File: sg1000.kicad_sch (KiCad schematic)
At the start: 76 parts, among them CN1 Conn_01x07_Female, J1 USB-B1HSB6, J2 RCJ-014, J3 RCJ-013, Q1 2n4401, Q1c1 2n3906, SW1 Pause Key, SW2 Power Toggle, SW3 Reset Key, U1 SG-1000-Cart, U100 74HCT574, U101 74HCT574, U102 74HCT574, U103 AS6C62256-DIP, U11 AS6C62256-DIP, U12 TMS9918A, U13 74LS139, U16 74LS32, U17 74LS14, U18 74LS257, U2 SG-1000-Expansion, U21 74LS257, U3 SN76489AN, U4 74LS32, U5 27C256, U6 74LS573, U7 74LS00, U9 Z80CPU, U99 74HCT04, X2 10.73863MHz

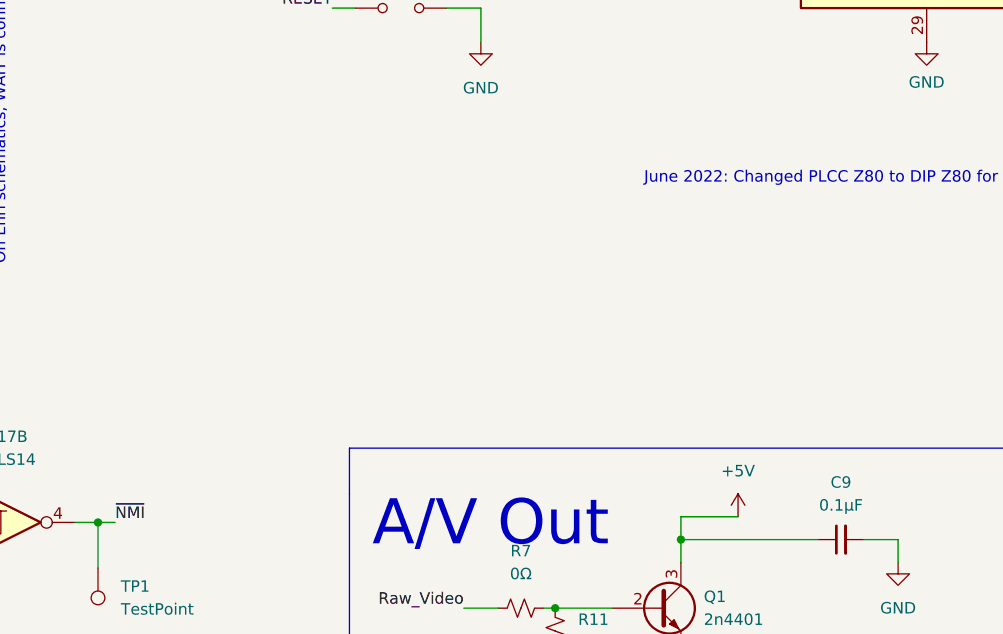
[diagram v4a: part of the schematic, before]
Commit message: Ground unused Schmitt trigger inputs
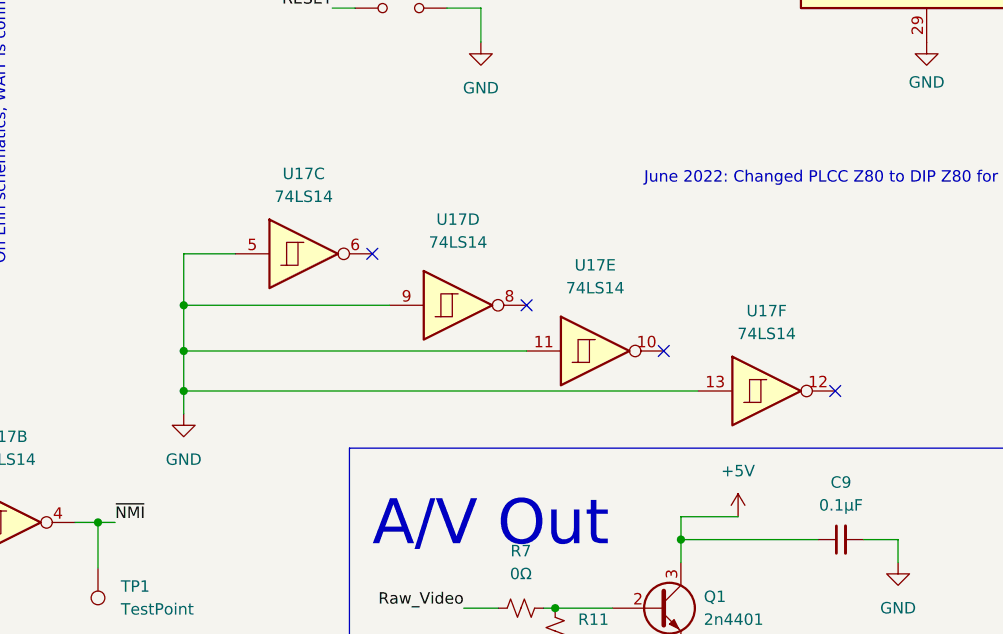
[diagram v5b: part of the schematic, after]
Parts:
- added unit 4 of U17
- added unit 6 of U17
- added unit 3 of U17
- added unit 5 of U17
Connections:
- net GND: now also U17.11, U17.13, U17.5, U17.9
- no-connect marks 25 -> 29
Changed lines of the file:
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@@
   (junction (at 219.71 165.735) (diameter 0) (color 0 0 0 0)
   )
+  (junction (at 229.235 146.685) (diameter 0) (color 0 0 0 0)
+  )
+  (junction (at 229.235 141.605) (diameter 0) (color 0 0 0 0)
+  )
   (junction (at 191.135 101.6) (diameter 0) (color 0 0 0 0)
   )
@@
   (junction (at 237.49 69.215) (diameter 0) (color 0 0 0 0)
   )
+  (junction (at 229.235 151.13) (diameter 0) (color 0 0 0 0)
+  )
   (junction (at 45.085 81.28) (diameter 0) (color 0 0 0 0)
   )
@@
   (no_connect (at 417.83 43.18))
   (no_connect (at 65.405 455.93))
+  (no_connect (at 282.575 146.685))
+  (no_connect (at 301.625 151.13))
+  (no_connect (at 267.335 141.605))
+  (no_connect (at 250.19 135.89))
   (no_connect (at 65.405 440.69))
   (no_connect (at 294.005 104.775))
@@
     (stroke (width 0) (type default) (color 0 0 0 0))
   )
+  (wire (pts (xy 229.235 135.89) (xy 229.235 141.605))
+    (stroke (width 0) (type default) (color 0 0 0 0))
+  )
   (wire (pts (xy 71.755 673.735) (xy 78.105 673.735))
     (stroke (width 0) (type default) (color 0 0 0 0))
@@
     (stroke (width 0) (type default) (color 0 0 0 0))
   )
+  (wire (pts (xy 229.235 151.13) (xy 286.385 151.13))
+    (stroke (width 0) (type default) (color 0 0 0 0))
+  )
   (wire (pts (xy 133.35 322.58) (xy 138.43 322.58))
     (stroke (width 0) (type default) (color 0 0 0 0))
@@
     (stroke (width 0) (type default) (color 0 0 0 0))
   )
+  (wire (pts (xy 234.95 135.89) (xy 229.235 135.89))
+    (stroke (width 0) (type default) (color 0 0 0 0))
+  )
   (wire (pts (xy 66.04 534.67) (xy 73.66 534.67))
     (stroke (width 0) (type default) (color 0 0 0 0))
   )
+  (wire (pts (xy 229.235 141.605) (xy 252.095 141.605))
+    (stroke (width 0) (type default) (color 0 0 0 0))
+  )
   (wire (pts (xy 60.96 40.005) (xy 55.245 40.005))
     (stroke (width 0) (type default) (color 0 0 0 0))
@@
     (stroke (width 0) (type default) (color 0 0 0 0))
   )
+  (wire (pts (xy 229.235 151.13) (xy 229.235 153.67))
+    (stroke (width 0) (type default) (color 0 0 0 0))
+  )
   (wire (pts (xy 149.225 746.125) (xy 149.225 748.665))
     (stroke (width 0) (type default) (color 0 0 0 0))
@@
     (stroke (width 0) (type default) (color 0 0 0 0))
   )
+  (wire (pts (xy 229.235 146.685) (xy 229.235 151.13))
+    (stroke (width 0) (type default) (color 0 0 0 0))
+  )
   (wire (pts (xy 269.24 175.26) (xy 270.51 175.26))
     (stroke (width 0) (type default) (color 0 0 0 0))
@@
     (stroke (width 0) (type default) (color 0 0 0 0))
   )
+  (wire (pts (xy 229.235 141.605) (xy 229.235 146.685))
+    (stroke (width 0) (type default) (color 0 0 0 0))
+  )
   (wire (pts (xy 153.67 443.23) (xy 137.795 443.23))
     (stroke (width 0) (type default) (color 0 0 0 0))
@@
     (stroke (width 0) (type default) (color 0 0 0 0))
   )
+  (wire (pts (xy 229.235 146.685) (xy 267.335 146.685))
+    (stroke (width 0) (type default) (color 0 0 0 0))
+  )
   (wire (pts (xy 43.815 668.655) (xy 51.435 668.655))
     (stroke (width 0) (type default) (color 0 0 0 0))
@@
     (pin "2")
   )
+  (symbol (lib_id "power:GND") (at 229.235 153.67 0) (unit 1)
+    (in_bom yes) (on_board yes) (fields_autoplaced)
+    (property "Reference" "#PWR?" (id 0) (at 229.235 160.02 0)
+      (effects (font (size 1.27 1.27)) hide)
+    )
+    (property "Value" "GND" (id 1) (at 229.235 158.75 0))
+    (property "Footprint" "" (id 2) (at 229.235 153.67 0)
+      (effects (font (size 1.27 1.27)) hide)
+    )
+    (property "Datasheet" "" (id 3) (at 229.235 153.67 0)
+      (effects (font (size 1.27 1.27)) hide)
+    )
+    (pin "1")
+  )
   (symbol (lib_id "power:+5V") (at 106.045 186.055 0) (unit 1)
     (in_bom yes) (on_board yes) (fields_autoplaced)
@@
     (pin "2")
   )
+  (symbol (lib_id "74xx:74LS14") (at 259.715 141.605 0) (unit 4)
+    (in_bom yes) (on_board yes) (fields_autoplaced)
+    (property "Reference" "U17" (id 0) (at 259.715 132.08 0))
+    (property "Value" "74LS14" (id 1) (at 259.715 134.62 0))
+    (property "Footprint" "" (id 2) (at 259.715 141.605 0)
+      (effects (font (size 1.27 1.27)) hide)
+    )
+    (property "Datasheet" "http://www.ti.com/lit/gpn/sn74LS14" (id 3) (at 259.715 141.605 0)
+      (effects (font (size 1.27 1.27)) hide)
+    )
+    (pin "8")
+    (pin "9")
+  )
   (symbol (lib_id "Device:R_Small_US") (at 450.85 58.42 90) (unit 1)
     (in_bom yes) (on_board yes) (fields_autoplaced)
@@
     (pin "2")
   )
+  (symbol (lib_id "74xx:74LS14") (at 294.005 151.13 0) (unit 6)
+    (in_bom yes) (on_board yes) (fields_autoplaced)
+    (property "Reference" "U17" (id 0) (at 294.005 142.24 0))
+    (property "Value" "74LS14" (id 1) (at 294.005 144.78 0))
+    (property "Footprint" "" (id 2) (at 294.005 151.13 0)
+      (effects (font (size 1.27 1.27)) hide)
+    )
+    (property "Datasheet" "http://www.ti.com/lit/gpn/sn74LS14" (id 3) (at 294.005 151.13 0)
+      (effects (font (size 1.27 1.27)) hide)
+    )
+    (pin "12")
+    (pin "13")
+  )
   (symbol (lib_id "power:+5V") (at 308.61 31.75 0) (unit 1)
     (in_bom yes) (on_board yes) (fields_autoplaced)
@@
     (pin "1")
   )
+  (symbol (lib_id "74xx:74LS14") (at 242.57 135.89 0) (unit 3)
+    (in_bom yes) (on_board yes) (fields_autoplaced)
+    (property "Reference" "U17" (id 0) (at 242.57 127 0))
+    (property "Value" "74LS14" (id 1) (at 242.57 129.54 0))
+    (property "Footprint" "" (id 2) (at 242.57 135.89 0)
+      (effects (font (size 1.27 1.27)) hide)
+    )
+    (property "Datasheet" "http://www.ti.com/lit/gpn/sn74LS14" (id 3) (at 242.57 135.89 0)
+      (effects (font (size 1.27 1.27)) hide)
+    )
+    (pin "5")
+    (pin "6")
+  )
   (symbol (lib_id "Device:R_Small_US") (at 284.48 185.42 0) (unit 1)
     (in_bom yes) (on_board yes) (fields_autoplaced)
@@
     (pin "2")
   )
+  (symbol (lib_id "74xx:74LS14") (at 274.955 146.685 0) (unit 5)
+    (in_bom yes) (on_board yes) (fields_autoplaced)
+    (property "Reference" "U17" (id 0) (at 274.955 137.16 0))
+    (property "Value" "74LS14" (id 1) (at 274.955 139.7 0))
+    (property "Footprint" "" (id 2) (at 274.955 146.685 0)
+      (effects (font (size 1.27 1.27)) hide)
+    )
+    (property "Datasheet" "http://www.ti.com/lit/gpn/sn74LS14" (id 3) (at 274.955 146.685 0)
+      (effects (font (size 1.27 1.27)) hide)
+    )
+    (pin "10")
+    (pin "11")
+  )
   (symbol (lib_id "74xx:74LS32") (at 100.965 601.345 0) (unit 3)
     (in_bom yes) (on_board yes) (fields_autoplaced)
@@
       (reference "#PWR0169") (unit 1) (value "GND") (footprint "")
     )
+    (path "/0e0f72eb-ced8-432d-b843-913cc8b0c274"
+      (reference "#PWR?") (unit 1) (value "GND") (footprint "")
+    )
     (path "/00000000-0000-0000-0000-00005e7d9a30"
       (reference "C1") (unit 1) (value "0.1µF") (footprint "Capacitor_SMD:C_0805_2012Metric_Pad1.15x1.40mm_HandSolder")
@@
       (reference "U17") (unit 2) (value "74LS14") (footprint "Package_DIP:DIP-14_W7.62mm_Socket_LongPads")
     )
+    (path "/9890ab0d-60be-401f-9610-601b07554a6a"
+      (reference "U17") (unit 3) (value "74LS14") (footprint "")
+    )
+    (path "/6402a45e-5c18-4acb-95d5-4d4add53b62f"
+      (reference "U17") (unit 4) (value "74LS14") (footprint "")
+    )
+    (path "/cabad2b3-d478-4de3-8c0a-6aca87ea2c66"
+      (reference "U17") (unit 5) (value "74LS14") (footprint "")
+    )
+    (path "/8e7b1928-223e-47d4-86c0-186f141f0453"
+      (reference "U17") (unit 6) (value "74LS14") (footprint "")
+    )
     (path "/7694c0b2-929f-4a6b-9d1a-50ef57c75725"

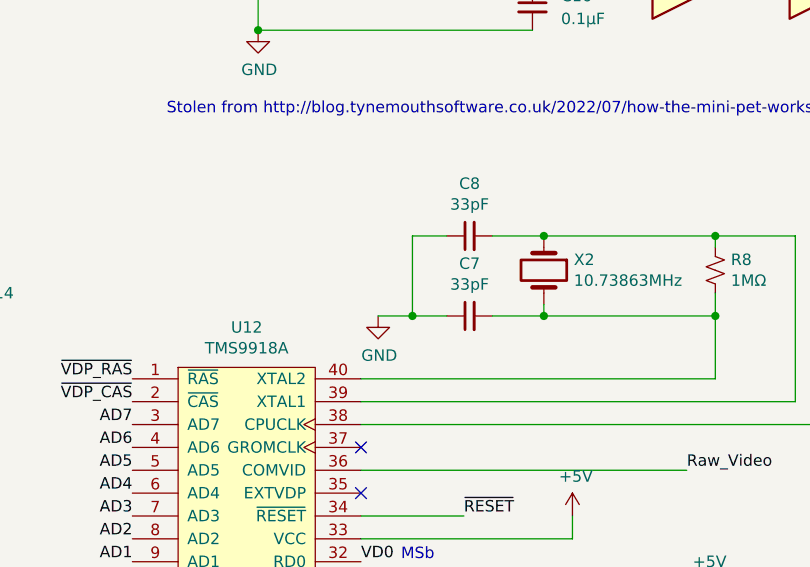
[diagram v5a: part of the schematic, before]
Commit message: Trim cap for clock crystal
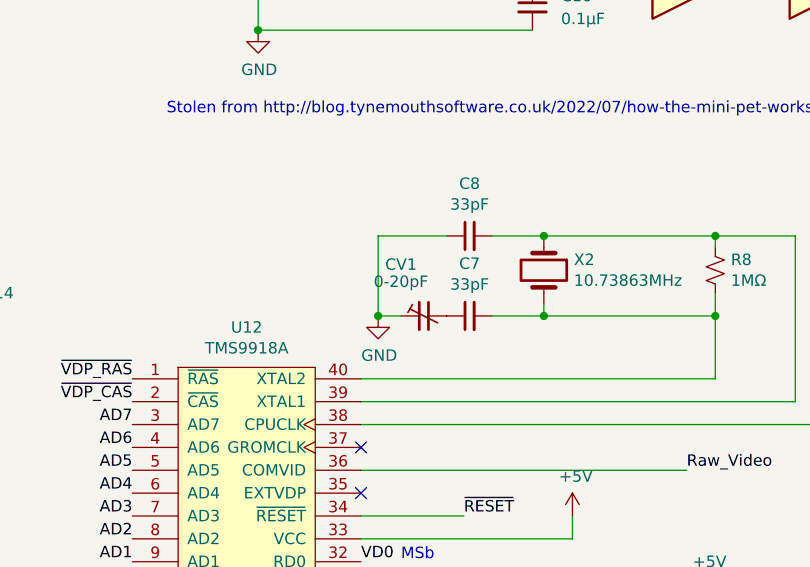
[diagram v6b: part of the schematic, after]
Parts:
- added CV1: 0-20pF, LeadedSolder:Tayda_Variable_Trimmer_Cap, symbol Device:C_Trim_Small
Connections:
- net GND: now also CV1.1; no longer C7.1
- new net: C7.1, CV1.2
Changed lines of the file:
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@@
   (junction (at 114.3 466.725) (diameter 0) (color 0 0 0 0)
   )
+  (junction (at 160.02 202.565) (diameter 0) (color 0 0 0 0)
+  )
   (junction (at 270.51 175.26) (diameter 0) (color 0 0 0 0)
   )
@@
   (junction (at 434.34 58.42) (diameter 0) (color 0 0 0 0)
   )
-  (junction (at 163.83 202.565) (diameter 0) (color 0 0 0 0)
-  )
   (junction (at 439.42 54.61) (diameter 0) (color 0 0 0 0)
   )
@@
     (stroke (width 0) (type default) (color 0 0 0 0))
   )
-  (wire (pts (xy 163.83 202.565) (xy 163.83 193.675))
-    (stroke (width 0) (type default) (color 0 0 0 0))
-  )
   (wire (pts (xy 25.4 182.245) (xy 29.21 182.245))
     (stroke (width 0) (type default) (color 0 0 0 0))
@@
     (stroke (width 0) (type default) (color 0 0 0 0))
   )
+  (wire (pts (xy 160.02 193.675) (xy 160.02 202.565))
+    (stroke (width 0) (type default) (color 0 0 0 0))
+  )
   (wire (pts (xy 464.82 58.42) (xy 458.47 58.42))
     (stroke (width 0) (type default) (color 0 0 0 0))
@@
     (stroke (width 0) (type default) (color 0 0 0 0))
   )
+  (wire (pts (xy 160.02 193.675) (xy 167.64 193.675))
+    (stroke (width 0) (type default) (color 0 0 0 0))
+  )
   (wire (pts (xy 35.56 547.37) (xy 43.18 547.37))
     (stroke (width 0) (type default) (color 0 0 0 0))
@@
     (stroke (width 0) (type default) (color 0 0 0 0))
   )
+  (wire (pts (xy 160.02 202.565) (xy 162.56 202.565))
+    (stroke (width 0) (type default) (color 0 0 0 0))
+  )
   (wire (pts (xy 270.51 175.26) (xy 276.86 175.26))
     (stroke (width 0) (type default) (color 0 0 0 0))
@@
     (stroke (width 0) (type default) (color 0 0 0 0))
   )
-  (wire (pts (xy 163.83 193.675) (xy 167.64 193.675))
-    (stroke (width 0) (type default) (color 0 0 0 0))
-  )
   (wire (pts (xy 155.575 396.24) (xy 166.37 396.24))
     (stroke (width 0) (type default) (color 0 0 0 0))
@@
     (stroke (width 0) (type default) (color 0 0 0 0))
   )
-  (wire (pts (xy 160.02 202.565) (xy 163.83 202.565))
-    (stroke (width 0) (type default) (color 0 0 0 0))
-  )
   (wire (pts (xy 71.755 658.495) (xy 78.105 658.495))
     (stroke (width 0) (type default) (color 0 0 0 0))
@@
     (stroke (width 0) (type default) (color 0 0 0 0))
   )
-  (wire (pts (xy 163.83 202.565) (xy 167.64 202.565))
-    (stroke (width 0) (type default) (color 0 0 0 0))
-  )
   (wire (pts (xy 170.18 78.74) (xy 167.005 78.74))
     (stroke (width 0) (type default) (color 0 0 0 0))
@@
   (symbol (lib_id "power:GND") (at 229.235 153.67 0) (unit 1)
     (in_bom yes) (on_board yes) (fields_autoplaced)
-    (property "Reference" "#PWR?" (id 0) (at 229.235 160.02 0)
+    (property "Reference" "#PWR0151" (id 0) (at 229.235 160.02 0)
       (effects (font (size 1.27 1.27)) hide)
     )
@@
     (pin "1")
   )
+  (symbol (lib_id "Device:C_Trim_Small") (at 165.1 202.565 90) (unit 1)
+    (in_bom yes) (on_board yes)
+    (property "Reference" "CV1" (id 0) (at 162.56 196.85 90))
+    (property "Value" "0-20pF" (id 1) (at 162.56 198.755 90))
+    (property "Footprint" "LeadedSolder:Tayda_Variable_Trimmer_Cap" (id 2) (at 165.1 202.565 0)
+      (effects (font (size 1.27 1.27)) hide)
+    )
+    (property "Datasheet" "~" (id 3) (at 165.1 202.565 0)
+      (effects (font (size 1.27 1.27)) hide)
+    )
+    (pin "1")
+    (pin "2")
+  )
   (symbol (lib_id "power:GND") (at 44.45 715.01 0) (unit 1)
     (in_bom yes) (on_board yes) (fields_autoplaced)
@@
       (reference "#PWR0150") (unit 1) (value "+5V") (footprint "")
     )
+    (path "/0e0f72eb-ced8-432d-b843-913cc8b0c274"
+      (reference "#PWR0151") (unit 1) (value "GND") (footprint "")
+    )
     (path "/7fa93b8d-6199-40ac-a4b9-d0ffd76e76bb"
       (reference "#PWR0152") (unit 1) (value "+5V") (footprint "")
@@
       (reference "#PWR0169") (unit 1) (value "GND") (footprint "")
     )
-    (path "/0e0f72eb-ced8-432d-b843-913cc8b0c274"
-      (reference "#PWR?") (unit 1) (value "GND") (footprint "")
-    )
     (path "/00000000-0000-0000-0000-00005e7d9a30"
       (reference "C1") (unit 1) (value "0.1µF") (footprint "Capacitor_SMD:C_0805_2012Metric_Pad1.15x1.40mm_HandSolder")
@@
       (reference "CN1") (unit 1) (value "Conn_01x07_Female") (footprint "Connector_PinHeader_2.54mm:PinHeader_1x07_P2.54mm_Vertical")
     )
+    (path "/43f6980a-490a-4a0d-8e55-437b028e76db"
+      (reference "CV1") (unit 1) (value "0-20pF") (footprint "LeadedSolder:Tayda_Variable_Trimmer_Cap")
+    )
     (path "/00000000-0000-0000-0000-00006219586d"

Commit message: Fix MAPPER_SELECT never loading the 574
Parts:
- U7: footprint Package_DIP:DIP-14_W7.62mm_Socket_LongPads -> (none)
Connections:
- net A13: now also U7.12; no longer U7.1, U7.2
- net ~{MAPPER_SELECT}: now also U7.1, U7.2; no longer U6.11 (Load)
- net MAPPER_SELECT: now reaches U7.6
- net MAPPER_SELECT: now also U6.11 (Load); no longer U7.12
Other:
- note added: "Dec. 2022: I don't know why I double-inverted this"
- note added: "Dec. 2022: Load is active-high, but ~{MAPPER_SELECT} is active-low. Inverted ~{MAPPER_SELECT}"
- note added: "TODO: Add the ferrite bead from Leako back in here"

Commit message: ACTUALLY invert mapper_sel instead of inverting it back again
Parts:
- removed unit 2 of U7
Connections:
- net MAPPER_SELECT: now also U7.3
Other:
- note added: "TODO: The trim cap should be on "XTAL1" - but is XTAL1 pin 40 or pin 39? TI's datasheet disagrees with itself, even on the same page!"
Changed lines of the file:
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@@
   (junction (at 33.02 232.41) (diameter 0) (color 0 0 0 0)
   )
-  (junction (at 49.53 800.1) (diameter 0) (color 0 0 0 0)
-  )
   (junction (at 80.01 582.93) (diameter 0) (color 0 0 0 0)
   )
@@
     (stroke (width 0) (type default) (color 0 0 0 0))
   )
-  (wire (pts (xy 50.8 797.56) (xy 49.53 797.56))
-    (stroke (width 0) (type default) (color 0 0 0 0))
-  )
   (wire (pts (xy 25.4 182.245) (xy 29.21 182.245))
     (stroke (width 0) (type default) (color 0 0 0 0))
@@
     (stroke (width 0) (type default) (color 0 0 0 0))
   )
-  (wire (pts (xy 49.53 797.56) (xy 49.53 800.1))
-    (stroke (width 0) (type default) (color 0 0 0 0))
-  )
   (wire (pts (xy 80.01 582.93) (xy 80.01 598.805))
     (stroke (width 0) (type default) (color 0 0 0 0))
@@
     (stroke (width 0) (type default) (color 0 0 0 0))
   )
-  (wire (pts (xy 49.53 802.64) (xy 49.53 800.1))
-    (stroke (width 0) (type default) (color 0 0 0 0))
-  )
   (wire (pts (xy 66.04 529.59) (xy 73.66 529.59))
     (stroke (width 0) (type default) (color 0 0 0 0))
@@
     (stroke (width 0) (type default) (color 0 0 0 0))
   )
+  (wire (pts (xy 49.53 800.1) (xy 66.04 800.1))
+    (stroke (width 0) (type default) (color 0 0 0 0))
+  )
   (wire (pts (xy 142.875 88.9) (xy 144.145 88.9))
     (stroke (width 0) (type default) (color 0 0 0 0))
@@
     (stroke (width 0) (type default) (color 0 0 0 0))
   )
-  (wire (pts (xy 50.8 802.64) (xy 49.53 802.64))
-    (stroke (width 0) (type default) (color 0 0 0 0))
-  )
   (wire (pts (xy 66.04 537.21) (xy 73.66 537.21))
     (stroke (width 0) (type default) (color 0 0 0 0))
@@
     (effects (font (size 5.0038 5.0038)) (justify left bottom))
   )
+  (text "TODO: The trim cap should be on \"XTAL1\" - but is XTAL1 pin 40 or pin 39?\nTI's datasheet disagrees with itself, even on the same page!"
+    (at 129.54 186.055 0)
+    (effects (font (size 1.27 1.27)) (justify left bottom))
+  )
   (text "CSCN4 = Mark III only, and it seems to\nbe shorted to B1 on real SG-1000 carts,\nso we're going to use this signal for\ncartridge detection."
     (at 85.09 520.7 0)
@@
     (pin "1")
   )
-  (symbol (lib_id "74xx:74LS00") (at 58.42 800.1 0) (unit 2)
-    (in_bom yes) (on_board yes) (fields_autoplaced)
-    (property "Reference" "U7" (id 0) (at 58.42 791.21 0))
-    (property "Value" "74LS00" (id 1) (at 58.42 793.75 0))
-    (property "Footprint" "" (id 2) (at 58.42 800.1 0)
-      (effects (font (size 1.27 1.27)) hide)
-    )
-    (property "Datasheet" "http://www.ti.com/lit/gpn/sn74ls00" (id 3) (at 58.42 800.1 0)
-      (effects (font (size 1.27 1.27)) hide)
-    )
-    (pin "4")
-    (pin "5")
-    (pin "6")
-  )
   (symbol (lib_id "Device:R_Small_US") (at 270.51 177.8 0) (unit 1)
     (in_bom yes) (on_board yes) (fields_autoplaced)
@@
       (reference "U7") (unit 1) (value "74LS00") (footprint "")
     )
-    (path "/2cc91a27-fb02-4e1b-b9b9-773cdccfd3c3"
-      (reference "U7") (unit 2) (value "74LS00") (footprint "")
-    )
     (path "/920d71ed-1df7-4d0c-878d-ae98833f7fee"
